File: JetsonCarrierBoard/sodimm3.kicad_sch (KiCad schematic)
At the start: 1 part

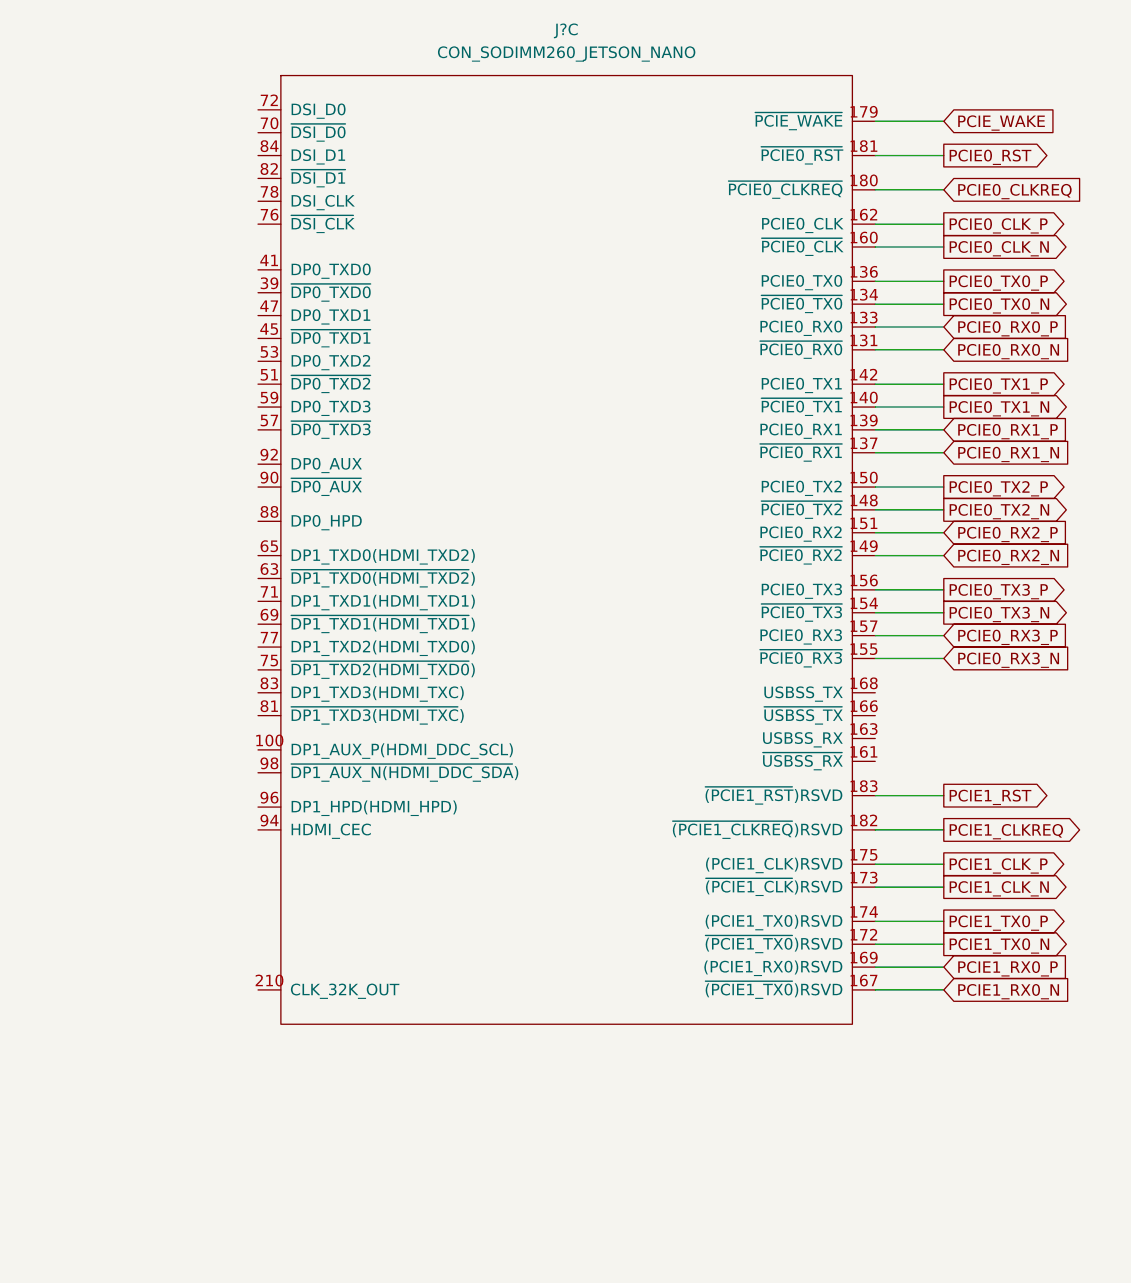
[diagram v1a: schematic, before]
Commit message: Finished USB-C w/ Alt mode and PD Wiring V1
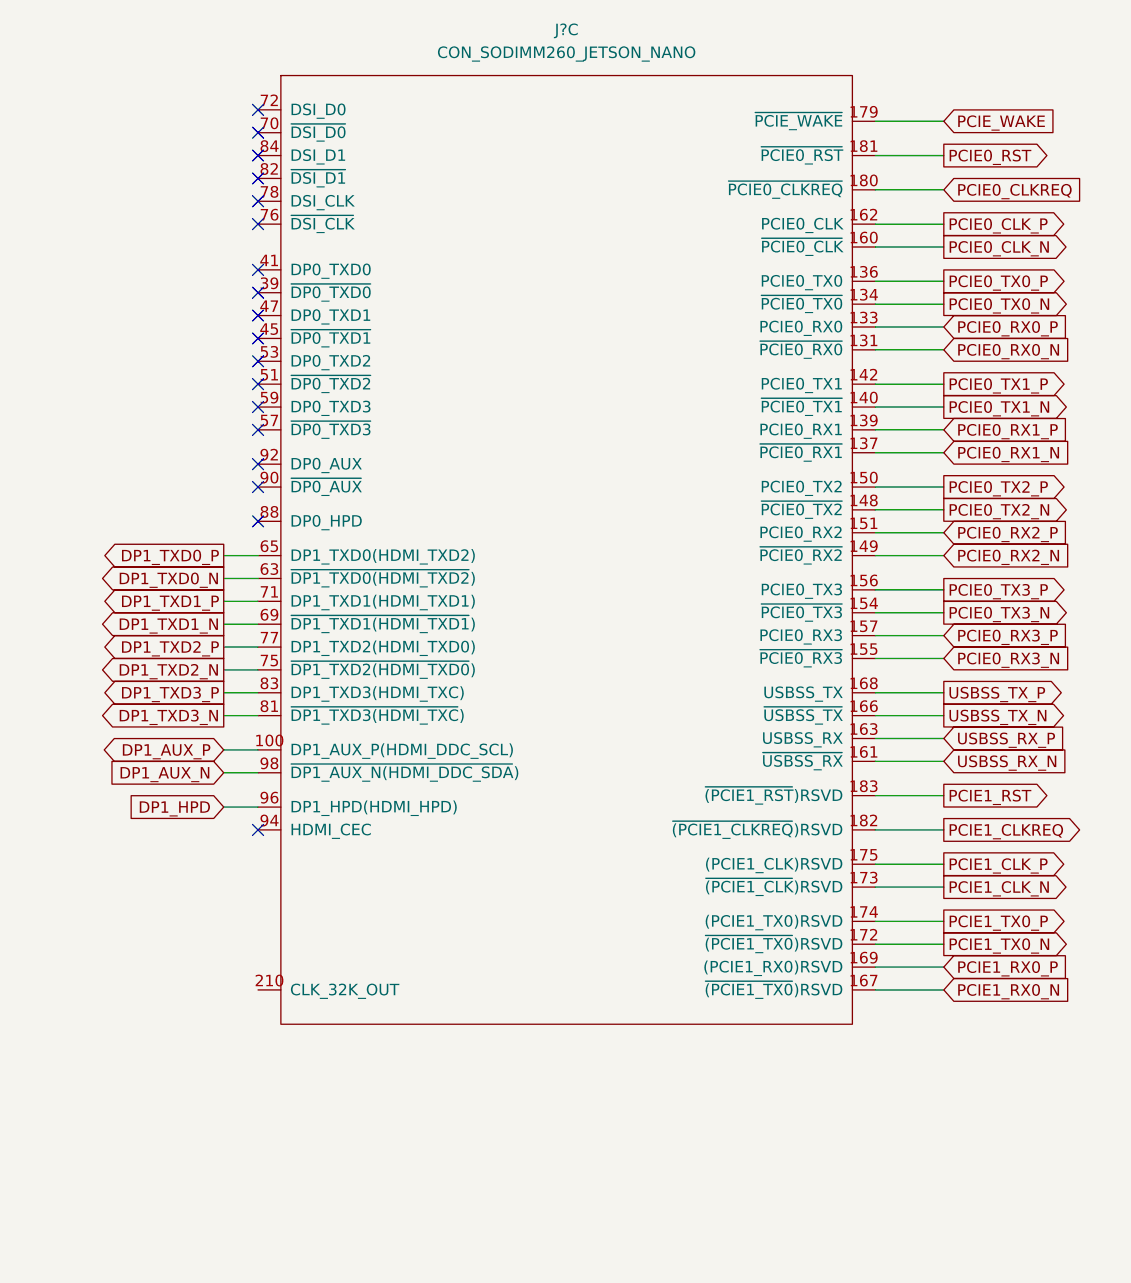
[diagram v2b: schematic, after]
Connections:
- net DP1_AUX_P: now reaches J?.100 (DP1_AUX_P(HDMI_DDC_SCL))
- net USBSS_RX_N: now reaches J?.161 (~{USBSS_RX})
- net USBSS_RX_P: now reaches J?.163 (USBSS_RX)
- net USBSS_TX_N: now reaches J?.166 (~{USBSS_TX})
- net USBSS_TX_P: now reaches J?.168 (USBSS_TX)
- net DP1_TXD0_N: now reaches J?.63 (~{DP1_TXD0(HDMI_TXD2}))
- net DP1_TXD0_P: now reaches J?.65 (DP1_TXD0(HDMI_TXD2))
- net DP1_TXD1_N: now reaches J?.69 (~{DP1_TXD1(HDMI_TXD1}))
- net DP1_TXD1_P: now reaches J?.71 (DP1_TXD1(HDMI_TXD1))
- net DP1_TXD2_N: now reaches J?.75 (~{DP1_TXD2(HDMI_TXD0}))
- net DP1_TXD2_P: now reaches J?.77 (DP1_TXD2(HDMI_TXD0))
- net DP1_TXD3_N: now reaches J?.81 (~{DP1_TXD3(HDMI_TXC}))
- net DP1_TXD3_P: now reaches J?.83 (DP1_TXD3(HDMI_TXC))
- net DP1_HPD: now reaches J?.96 (DP1_HPD(HDMI_HPD))
- net DP1_AUX_N: now reaches J?.98 (~{DP1_AUX_N(HDMI_DDC_SDA}))
- no-connect marks 0 -> 18

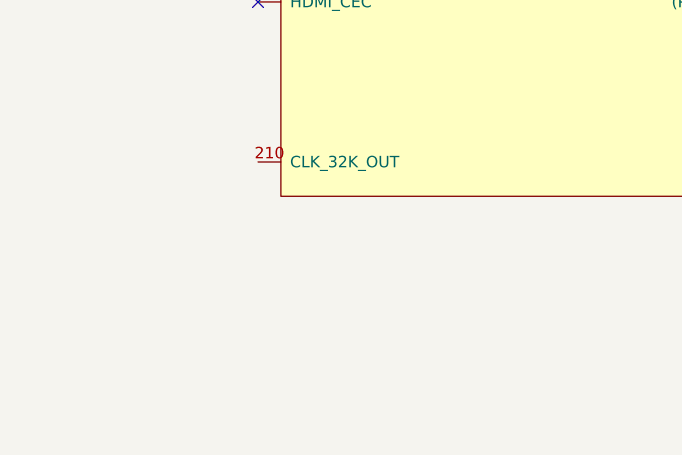
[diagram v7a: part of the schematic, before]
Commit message: IMU wiring
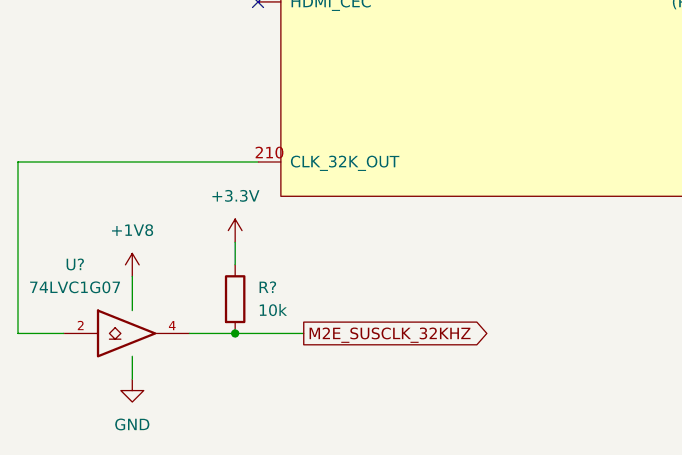
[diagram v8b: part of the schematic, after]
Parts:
- added R?: 10k, symbol Device:R
- added U?: 74LVC1G07, symbol 74xGxx:74LVC1G07
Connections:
- net at J?.210 (CLK_32K_OUT): now also U?.2
- new net +1V8: U?.5 (VCC)
- new net +3.3V: R?.1
- new net GND: U?.3 (GND)
- new net M2E_SUSCLK_32KHZ: R?.2, U?.4
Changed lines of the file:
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@@
 (kicad_sch (version 20211123) (generator eeschema)
   (paper "A4")
+  (junction (at 93.98 165.1) (diameter 0) (color 0 0 0 0)
+  )
   (no_connect (at 96.52 93.98))
   (no_connect (at 96.52 55.88))
@@
     (stroke (width 0) (type default) (color 0 0 0 0))
   )
+  (wire (pts (xy 96.52 146.05) (xy 69.85 146.05))
+    (stroke (width 0) (type default) (color 0 0 0 0))
+  )
   (wire (pts (xy 165.1 128.27) (xy 172.72 128.27))
     (stroke (width 0) (type default) (color 0 0 0 0))
@@
     (stroke (width 0) (type default) (color 0 0 0 0))
   )
+  (wire (pts (xy 93.98 165.1) (xy 101.6 165.1))
+    (stroke (width 0) (type default) (color 0 0 0 0))
+  )
   (wire (pts (xy 92.71 102.87) (xy 96.52 102.87))
     (stroke (width 0) (type default) (color 0 0 0 0))
@@
     (stroke (width 0) (type default) (color 0 0 0 0))
   )
+  (wire (pts (xy 82.55 167.64) (xy 82.55 170.18))
+    (stroke (width 0) (type default) (color 0 0 0 0))
+  )
   (wire (pts (xy 165.1 78.74) (xy 172.72 78.74))
     (stroke (width 0) (type default) (color 0 0 0 0))
@@
     (stroke (width 0) (type default) (color 0 0 0 0))
   )
+  (wire (pts (xy 69.85 165.1) (xy 74.93 165.1))
+    (stroke (width 0) (type default) (color 0 0 0 0))
+  )
+  (wire (pts (xy 93.98 154.94) (xy 93.98 157.48))
+    (stroke (width 0) (type default) (color 0 0 0 0))
+  )
   (wire (pts (xy 92.71 105.41) (xy 96.52 105.41))
     (stroke (width 0) (type default) (color 0 0 0 0))
@@
     (stroke (width 0) (type default) (color 0 0 0 0))
   )
+  (wire (pts (xy 88.9 165.1) (xy 93.98 165.1))
+    (stroke (width 0) (type default) (color 0 0 0 0))
+  )
   (wire (pts (xy 165.1 57.15) (xy 172.72 57.15))
     (stroke (width 0) (type default) (color 0 0 0 0))
   )
+  (wire (pts (xy 69.85 146.05) (xy 69.85 165.1))
+    (stroke (width 0) (type default) (color 0 0 0 0))
+  )
+  (wire (pts (xy 82.55 158.75) (xy 82.55 162.56))
+    (stroke (width 0) (type default) (color 0 0 0 0))
+  )
   (wire (pts (xy 165.1 124.46) (xy 172.72 124.46))
     (stroke (width 0) (type default) (color 0 0 0 0))
@@
   (wire (pts (xy 165.1 118.11) (xy 172.72 118.11))
     (stroke (width 0) (type default) (color 0 0 0 0))
+  )
+  (global_label "M2E_SUSCLK_32KHZ" (shape output) (at 101.6 165.1 0) (fields_autoplaced)
+    (effects (font (size 1.27 1.27)) (justify left))
+    (property "Intersheet References" "${INTERSHEET_REFS}" (id 0) (at 123.305 165.0206 0)
+      (effects (font (size 1.27 1.27)) (justify left) hide)
+    )
   )
   (global_label "PCIE1_TX0_N" (shape output) (at 172.72 140.97 0) (fields_autoplaced)
@@
     (pin "98")
   )
+  (symbol (lib_id "power:+3.3V") (at 93.98 154.94 0) (unit 1)
+    (in_bom yes) (on_board yes) (fields_autoplaced)
+    (property "Reference" "#PWR?" (id 0) (at 93.98 158.75 0)
+      (effects (font (size 1.27 1.27)) hide)
+    )
+    (property "Value" "+3.3V" (id 1) (at 93.98 149.86 0))
+    (property "Footprint" "" (id 2) (at 93.98 154.94 0)
+      (effects (font (size 1.27 1.27)) hide)
+    )
+    (property "Datasheet" "" (id 3) (at 93.98 154.94 0)
+      (effects (font (size 1.27 1.27)) hide)
+    )
+    (pin "1")
+  )
+  (symbol (lib_id "74xGxx:74LVC1G07") (at 82.55 165.1 0) (unit 1)
+    (in_bom yes) (on_board yes)
+    (property "Reference" "U?" (id 0) (at 76.2 157.48 0))
+    (property "Value" "74LVC1G07" (id 1) (at 76.2 160.02 0))
+    (property "Footprint" "" (id 2) (at 82.55 165.1 0)
+      (effects (font (size 1.27 1.27)) hide)
+    )
+    (property "Datasheet" "http://www.ti.com/lit/sg/scyt129e/scyt129e.pdf" (id 3) (at 82.55 165.1 0)
+      (effects (font (size 1.27 1.27)) hide)
+    )
+    (pin "2")
+    (pin "3")
+    (pin "4")
+    (pin "5")
+  )
+  (symbol (lib_id "Device:R") (at 93.98 161.29 0) (unit 1)
+    (in_bom yes) (on_board yes) (fields_autoplaced)
+    (property "Reference" "R?" (id 0) (at 96.52 160.0199 0)
+      (effects (font (size 1.27 1.27)) (justify left))
+    )
+    (property "Value" "10k" (id 1) (at 96.52 162.5599 0)
+      (effects (font (size 1.27 1.27)) (justify left))
+    )
+    (property "Footprint" "" (id 2) (at 92.202 161.29 90)
+      (effects (font (size 1.27 1.27)) hide)
+    )
+    (property "Datasheet" "~" (id 3) (at 93.98 161.29 0)
+      (effects (font (size 1.27 1.27)) hide)
+    )
+    (pin "1")
+    (pin "2")
+  )
+  (symbol (lib_id "power:+1V8") (at 82.55 158.75 0) (unit 1)
+    (in_bom yes) (on_board yes) (fields_autoplaced)
+    (property "Reference" "#PWR?" (id 0) (at 82.55 162.56 0)
+      (effects (font (size 1.27 1.27)) hide)
+    )
+    (property "Value" "+1V8" (id 1) (at 82.55 153.67 0))
+    (property "Footprint" "" (id 2) (at 82.55 158.75 0)
+      (effects (font (size 1.27 1.27)) hide)
+    )
+    (property "Datasheet" "" (id 3) (at 82.55 158.75 0)
+      (effects (font (size 1.27 1.27)) hide)
+    )
+    (pin "1")
+  )
+  (symbol (lib_id "power:GND") (at 82.55 170.18 0) (unit 1)
+    (in_bom yes) (on_board yes) (fields_autoplaced)
+    (property "Reference" "#PWR?" (id 0) (at 82.55 176.53 0)
+      (effects (font (size 1.27 1.27)) hide)
+    )
+    (property "Value" "GND" (id 1) (at 82.55 175.26 0))
+    (property "Footprint" "" (id 2) (at 82.55 170.18 0)
+      (effects (font (size 1.27 1.27)) hide)
+    )
+    (property "Datasheet" "" (id 3) (at 82.55 170.18 0)
+      (effects (font (size 1.27 1.27)) hide)
+    )
+    (pin "1")
+  )
 )
